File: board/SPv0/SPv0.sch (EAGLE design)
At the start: 52 parts, among them IC1 S34ML0XG1, IC2 F55[0/1]X---PT48, IC3 LM339D, Q1 12MHz, T1 n3904, T2 n3904, T3 n3906, T4 n3906, T5 n3906

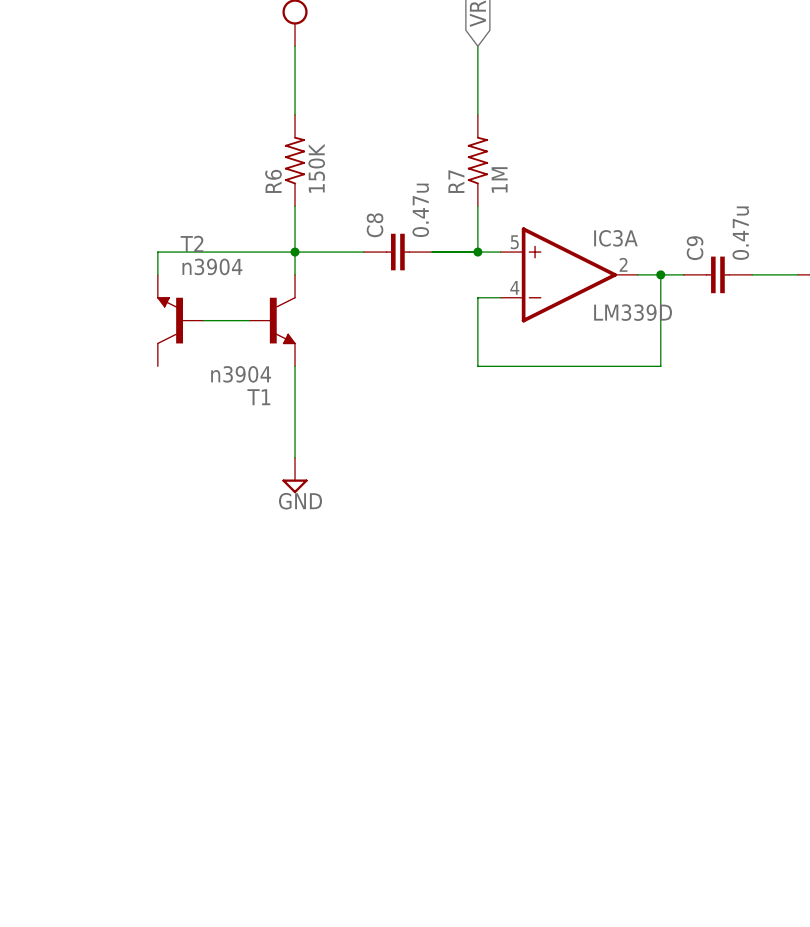
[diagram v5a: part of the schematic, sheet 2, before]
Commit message: removed obvious ERC problems
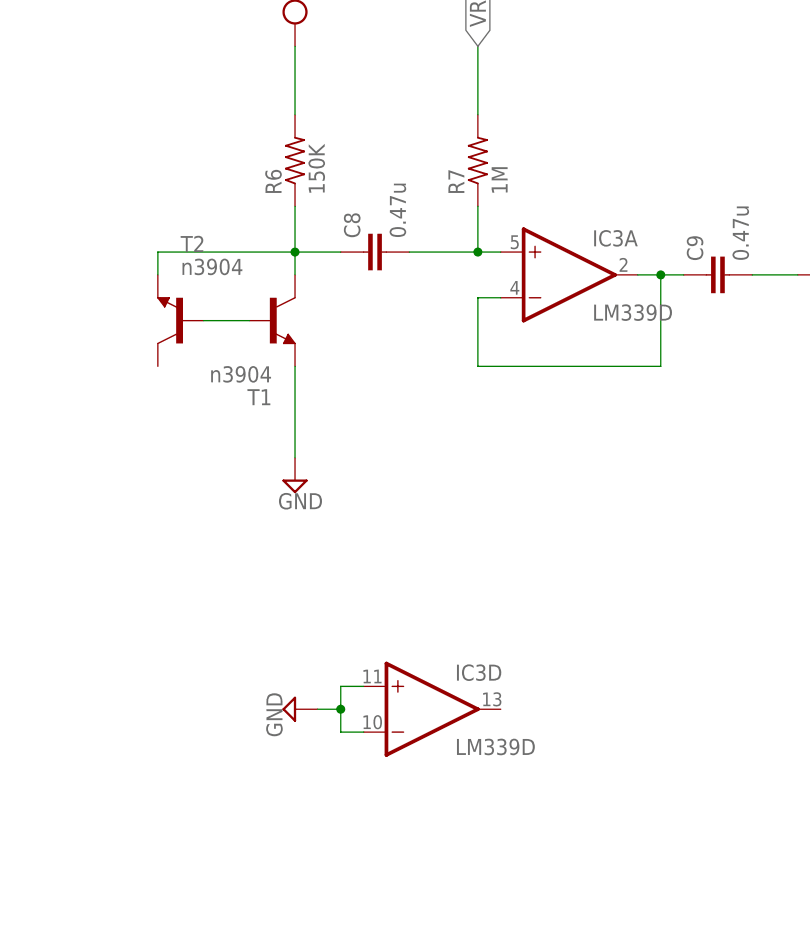
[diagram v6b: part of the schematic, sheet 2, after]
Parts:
- added C14: 470nF, rcl:C-EUC0805
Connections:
- new net N$3: C14.1, IC2.13
- net +3V3_A: now also IC2.7
- net GND: now also C14.2, IC2.10, IC2.44, IC3D.+IN, IC3D.-IN
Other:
- moved on the sheet: C8
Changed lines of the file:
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@@
 <part name="SUPPLY26" library="supply2" deviceset="VCC" device=""/>
 <part name="SUPPLY27" library="supply2" deviceset="VCC" device=""/>
+<part name="C14" library="rcl" deviceset="C-EU" device="C0805" value="470nF"/>
+<part name="SUPPLY18" library="supply2" deviceset="GND" device=""/>
+<part name="SUPPLY19" library="supply2" deviceset="GND" device=""/>
 </parts>
 <sheets>
@@
 <instance part="JTAG_A" gate="G$1" x="96.52" y="43.18"/>
 <instance part="SUPPLY27" gate="G$1" x="134.62" y="116.84" rot="R270"/>
+<instance part="C14" gate="G$1" x="5.08" y="86.36" rot="R270"/>
+<instance part="SUPPLY18" gate="GND" x="-5.08" y="86.36" rot="R270"/>
 </instances>
 <busses>
@@
 <label x="106.68" y="45.72" size="1.4224" layer="95"/>
 </segment>
+<segment>
+<pinref part="IC2" gate="G$1" pin="10"/>
+<wire x1="22.86" y1="93.98" x2="15.24" y2="93.98" width="0.1524" layer="91"/>
+<label x="15.24" y="93.98" size="1.4224" layer="95"/>
+</segment>
+<segment>
+<pinref part="IC2" gate="G$1" pin="44"/>
+<wire x1="73.66" y1="106.68" x2="81.28" y2="106.68" width="0.1524" layer="91"/>
+<label x="76.2" y="106.68" size="1.4224" layer="95"/>
+</segment>
+<segment>
+<pinref part="SUPPLY18" gate="GND" pin="GND"/>
+<pinref part="C14" gate="G$1" pin="2"/>
+<wire x1="-2.54" y1="86.36" x2="0" y2="86.36" width="0.1524" layer="91"/>
+</segment>
 </net>
 <net name="+3V3_A" class="0">
@@
 <wire x1="88.9" y1="35.56" x2="83.82" y2="35.56" width="0.1524" layer="91"/>
 <label x="83.82" y="35.56" size="1.4224" layer="95"/>
+</segment>
+<segment>
+<pinref part="IC2" gate="G$1" pin="7"/>
+<wire x1="22.86" y1="101.6" x2="15.24" y2="101.6" width="0.1524" layer="91"/>
+<label x="15.24" y="101.6" size="1.4224" layer="95"/>
 </segment>
 </net>
@@
 <pinref part="SUPPLY27" gate="G$1" pin="VCC"/>
 <wire x1="127" y1="116.84" x2="132.08" y2="116.84" width="0.1524" layer="91"/>
+</segment>
+</net>
+<net name="N$3" class="0">
+<segment>
+<pinref part="C14" gate="G$1" pin="1"/>
+<pinref part="IC2" gate="G$1" pin="13"/>
+<wire x1="7.62" y1="86.36" x2="22.86" y2="86.36" width="0.1524" layer="91"/>
 </segment>
 </net>
@@
 <instance part="IC3" gate="A" x="139.7" y="78.74"/>
 <instance part="IC3" gate="B" x="187.96" y="81.28"/>
-<instance part="C8" gate="G$1" x="119.38" y="81.28" rot="R90"/>
+<instance part="C8" gate="G$1" x="116.84" y="81.28" rot="R90"/>
 <instance part="C9" gate="G$1" x="154.94" y="78.74" rot="R90"/>
 <instance part="R8" gate="G$1" x="170.18" y="78.74"/>
@@
 <instance part="SUPPLY22" gate="G$1" x="172.72" y="43.18"/>
 <instance part="SUPPLY23" gate="G$1" x="109.22" y="106.68"/>
+<instance part="IC3" gate="D" x="124.46" y="30.48"/>
+<instance part="SUPPLY19" gate="GND" x="109.22" y="30.48" rot="R270"/>
 </instances>
 <busses>
@@
 <pinref part="SUPPLY17" gate="GND" pin="GND"/>
 <wire x1="172.72" y1="20.32" x2="172.72" y2="17.78" width="0.1524" layer="91"/>
+</segment>
+<segment>
+<pinref part="IC3" gate="D" pin="+IN"/>
+<wire x1="116.84" y1="33.02" x2="114.3" y2="33.02" width="0.1524" layer="91"/>
+<wire x1="114.3" y1="33.02" x2="114.3" y2="30.48" width="0.1524" layer="91"/>
+<pinref part="IC3" gate="D" pin="-IN"/>
+<wire x1="114.3" y1="30.48" x2="114.3" y2="27.94" width="0.1524" layer="91"/>
+<wire x1="114.3" y1="27.94" x2="116.84" y2="27.94" width="0.1524" layer="91"/>
+<pinref part="SUPPLY19" gate="GND" pin="GND"/>
+<wire x1="111.76" y1="30.48" x2="114.3" y2="30.48" width="0.1524" layer="91"/>
+<junction x="114.3" y="30.48"/>
 </segment>
 </net>
@@
 <junction x="109.22" y="81.28"/>
 <pinref part="C8" gate="G$1" pin="1"/>
-<wire x1="109.22" y1="81.28" x2="116.84" y2="81.28" width="0.1524" layer="91"/>
+<wire x1="109.22" y1="81.28" x2="114.3" y2="81.28" width="0.1524" layer="91"/>
 </segment>
 </net>
@@
 <net name="N$7" class="0">
 <segment>
-<pinref part="C8" gate="G$1" pin="2"/>
 <pinref part="IC3" gate="A" pin="+IN"/>
-<wire x1="124.46" y1="81.28" x2="129.54" y2="81.28" width="0.1524" layer="91"/>
 <pinref part="R7" gate="G$1" pin="1"/>
 <wire x1="129.54" y1="81.28" x2="132.08" y2="81.28" width="0.1524" layer="91"/>
 <wire x1="129.54" y1="86.36" x2="129.54" y2="81.28" width="0.1524" layer="91"/>
+<pinref part="C8" gate="G$1" pin="2"/>
+<wire x1="121.92" y1="81.28" x2="129.54" y2="81.28" width="0.1524" layer="91"/>
 <junction x="129.54" y="81.28"/>
-<wire x1="124.46" y1="81.28" x2="129.54" y2="81.28" width="0.1524" layer="91"/>
-</segment>
-</net>
+</segment>
+</net>

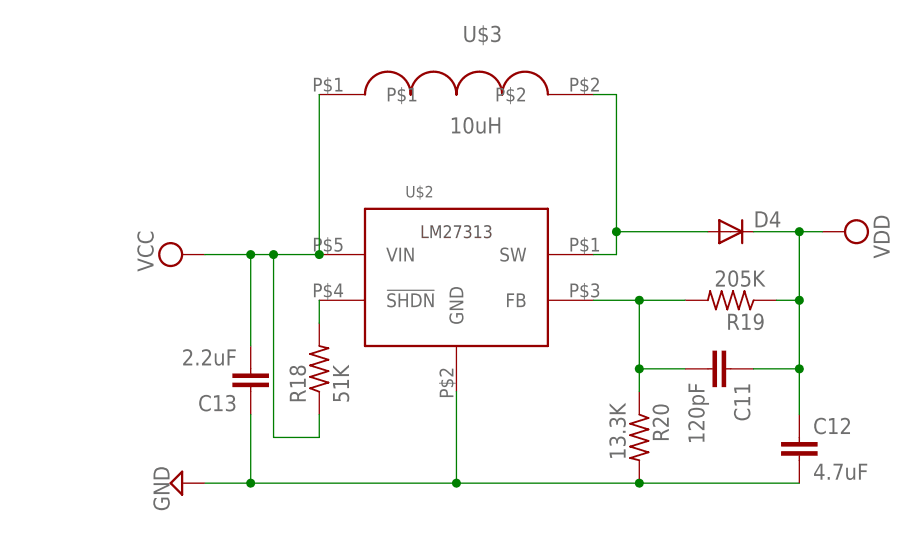
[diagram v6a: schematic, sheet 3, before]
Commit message: layout of rng in good shape
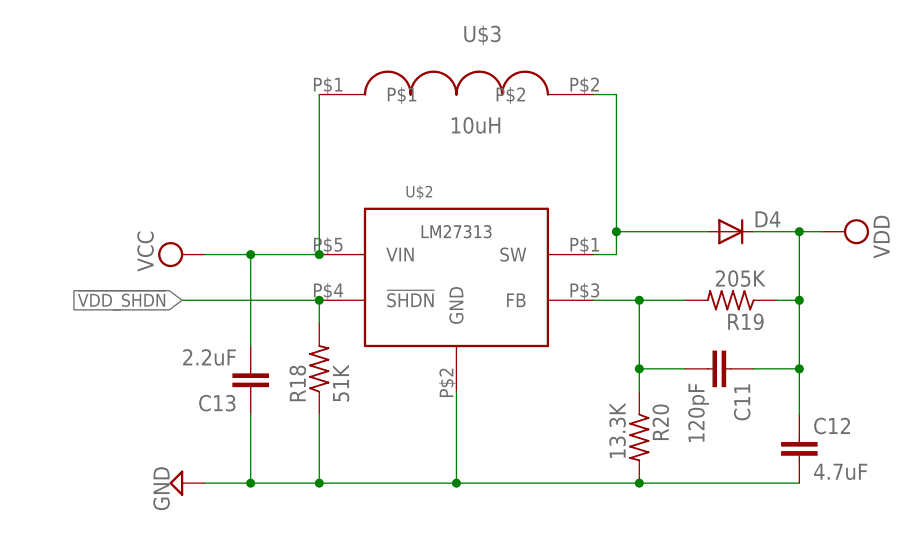
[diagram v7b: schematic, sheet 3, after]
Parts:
- R10, R11, R12, R13, R14, R15, R16, R17, R6, R7, R8, R9: device rcl:R-US_R0805 -> rcl:R-US_R0603
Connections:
- removed net DOUT_1: R16.1, R17.2, TP2.TP
- removed net N$19: R18.2, U$2.!SHDN!
- new net !VDD_SHDN!: IC2.2, R18.2, U$2.!SHDN!
- new net DOUT: IC2.1, R16.1, R17.2, TP2.TP
- net GND: now also R18.1
- net VCC: no longer R18.1
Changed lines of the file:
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@@
 <part name="T1" library="transistor" deviceset="*-NPN-" device="SOT23-BEC" technology="MMBT3904LT1" value="n3904"/>
 <part name="T2" library="transistor" deviceset="*-NPN-" device="SOT23-BEC" technology="MMBT3904LT1" value="n3904"/>
-<part name="R6" library="rcl" deviceset="R-US_" device="R0805" value="150K"/>
-<part name="R7" library="rcl" deviceset="R-US_" device="R0805" value="1M"/>
+<part name="R6" library="rcl" deviceset="R-US_" device="R0603" value="150K"/>
+<part name="R7" library="rcl" deviceset="R-US_" device="R0603" value="1M"/>
 <part name="SUPPLY11" library="supply2" deviceset="GND" device=""/>
 <part name="IC3" library="linear" deviceset="LM339" device="D"/>
 <part name="C8" library="rcl" deviceset="C-EU" device="C0805" value="0.47u"/>
 <part name="C9" library="rcl" deviceset="C-EU" device="C0805" value="0.47u"/>
-<part name="R8" library="rcl" deviceset="R-US_" device="R0805" value="12K"/>
-<part name="R9" library="rcl" deviceset="R-US_" device="R0805" value="47K"/>
-<part name="R10" library="rcl" deviceset="R-US_" device="R0805" value="1M"/>
+<part name="R8" library="rcl" deviceset="R-US_" device="R0603" value="12K"/>
+<part name="R9" library="rcl" deviceset="R-US_" device="R0603" value="47K"/>
+<part name="R10" library="rcl" deviceset="R-US_" device="R0603" value="1M"/>
 <part name="SUPPLY12" library="supply2" deviceset="GND" device=""/>
 <part name="SUPPLY13" library="supply2" deviceset="GND" device=""/>
 <part name="C10" library="rcl" deviceset="C-EU" device="C0805" value="4.7u"/>
-<part name="R11" library="rcl" deviceset="R-US_" device="R0805" value="100K"/>
-<part name="R12" library="rcl" deviceset="R-US_" device="R0805" value="100K"/>
+<part name="R11" library="rcl" deviceset="R-US_" device="R0603" value="100K"/>
+<part name="R12" library="rcl" deviceset="R-US_" device="R0603" value="100K"/>
 <part name="T3" library="transistor" deviceset="*-PNP-" device="SOT23-BEC" technology="MMBT3906LT1" value="n3906"/>
 <part name="T4" library="transistor" deviceset="*-PNP-" device="SOT23-BEC" technology="MMBT3906LT1" value="n3906"/>
 <part name="T5" library="transistor" deviceset="*-PNP-" device="SOT23-BEC" technology="MMBT3906LT1" value="n3906"/>
-<part name="R13" library="rcl" deviceset="R-US_" device="R0805" value="1.2K"/>
-<part name="R14" library="rcl" deviceset="R-US_" device="R0805" value="10K"/>
-<part name="R15" library="rcl" deviceset="R-US_" device="R0805" value="10K"/>
-<part name="R16" library="rcl" deviceset="R-US_" device="R0805" value="5K"/>
-<part name="R17" library="rcl" deviceset="R-US_" device="R0805" value="5K"/>
+<part name="R13" library="rcl" deviceset="R-US_" device="R0603" value="1.2K"/>
+<part name="R14" library="rcl" deviceset="R-US_" device="R0603" value="10K"/>
+<part name="R15" library="rcl" deviceset="R-US_" device="R0603" value="10K"/>
+<part name="R16" library="rcl" deviceset="R-US_" device="R0603" value="5K"/>
+<part name="R17" library="rcl" deviceset="R-US_" device="R0603" value="5K"/>
 <part name="D2" library="zetex" deviceset="D" device="SOD323"/>
 <part name="D3" library="zetex" deviceset="D" device="SOD323"/>
@@
 <text x="17.78" y="106.68" size="1.4224" layer="91">RNG</text>
 <text x="17.78" y="104.14" size="1.4224" layer="91">RNG</text>
-<text x="17.78" y="116.84" size="1.4224" layer="91">RNG</text>
-<text x="17.78" y="114.3" size="1.4224" layer="91">RNG</text>
 </plain>
 <instances>
@@
 <pinref part="IC2" gate="G$1" pin="13"/>
 <wire x1="7.62" y1="86.36" x2="22.86" y2="86.36" width="0.1524" layer="91"/>
+</segment>
+</net>
+<net name="DOUT" class="0">
+<segment>
+<pinref part="IC2" gate="G$1" pin="1"/>
+<wire x1="22.86" y1="116.84" x2="15.24" y2="116.84" width="0.1524" layer="91"/>
+<label x="15.24" y="116.84" size="1.4224" layer="95"/>
+</segment>
+</net>
+<net name="!VDD_SHDN!" class="0">
+<segment>
+<pinref part="IC2" gate="G$1" pin="2"/>
+<wire x1="22.86" y1="114.3" x2="15.24" y2="114.3" width="0.1524" layer="91"/>
+<label x="15.24" y="114.3" size="1.4224" layer="95"/>
 </segment>
 </net>
@@
 </segment>
 </net>
-<net name="DOUT_1" class="0">
+<net name="DOUT" class="0">
 <segment>
 <pinref part="R17" gate="G$1" pin="2"/>
@@
 <wire x1="15.24" y1="35.56" x2="15.24" y2="25.4" width="0.1524" layer="91"/>
 <junction x="15.24" y="35.56"/>
-<pinref part="R18" gate="G$1" pin="1"/>
-<wire x1="22.86" y1="17.78" x2="22.86" y2="15.24" width="0.1524" layer="91"/>
-<wire x1="22.86" y1="15.24" x2="17.78" y2="15.24" width="0.1524" layer="91"/>
-<wire x1="17.78" y1="15.24" x2="17.78" y2="35.56" width="0.1524" layer="91"/>
-<junction x="17.78" y="35.56"/>
 <pinref part="U$3" gate="G$1" pin="P$1"/>
 <wire x1="22.86" y1="53.34" x2="22.86" y2="35.56" width="0.1524" layer="91"/>
@@
 <wire x1="10.16" y1="10.16" x2="15.24" y2="10.16" width="0.1524" layer="91"/>
 <pinref part="C12" gate="G$1" pin="2"/>
-<wire x1="15.24" y1="10.16" x2="38.1" y2="10.16" width="0.1524" layer="91"/>
+<wire x1="15.24" y1="10.16" x2="22.86" y2="10.16" width="0.1524" layer="91"/>
+<wire x1="22.86" y1="10.16" x2="38.1" y2="10.16" width="0.1524" layer="91"/>
 <wire x1="38.1" y1="10.16" x2="58.42" y2="10.16" width="0.1524" layer="91"/>
 <wire x1="58.42" y1="10.16" x2="76.2" y2="10.16" width="0.1524" layer="91"/>
@@
 <wire x1="15.24" y1="17.78" x2="15.24" y2="10.16" width="0.1524" layer="91"/>
 <junction x="15.24" y="10.16"/>
-</segment>
-</net>
-<net name="N$19" class="0">
+<pinref part="R18" gate="G$1" pin="1"/>
+<wire x1="22.86" y1="17.78" x2="22.86" y2="10.16" width="0.1524" layer="91"/>
+<junction x="22.86" y="10.16"/>
+</segment>
+</net>
+<net name="!VDD_SHDN!" class="0">
 <segment>
 <pinref part="U$2" gate="G$1" pin="!SHDN!"/>
 <pinref part="R18" gate="G$1" pin="2"/>
 <wire x1="22.86" y1="30.48" x2="22.86" y2="27.94" width="0.1524" layer="91"/>
-</segment>
-</net>
+<wire x1="22.86" y1="30.48" x2="7.62" y2="30.48" width="0.1524" layer="91"/>
+<junction x="22.86" y="30.48"/>
+<label x="7.62" y="30.48" size="1.4224" layer="95" rot="R180" xref="yes"/>
+</segment>
+</net>
